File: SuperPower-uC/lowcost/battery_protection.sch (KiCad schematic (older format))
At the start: 7 parts, among them J1 Battery connector, J7 Battery connector, U1 FS312F-G, U2 FS8205A

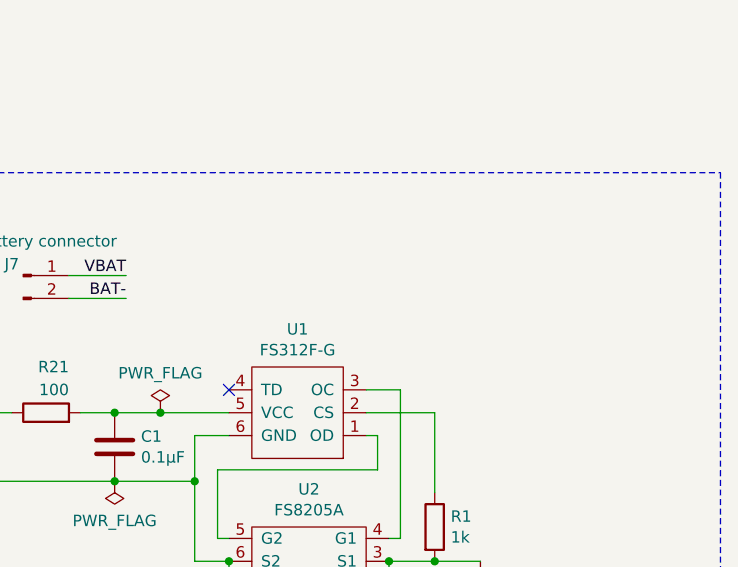
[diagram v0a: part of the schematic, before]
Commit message: added jumper to skip battery protection
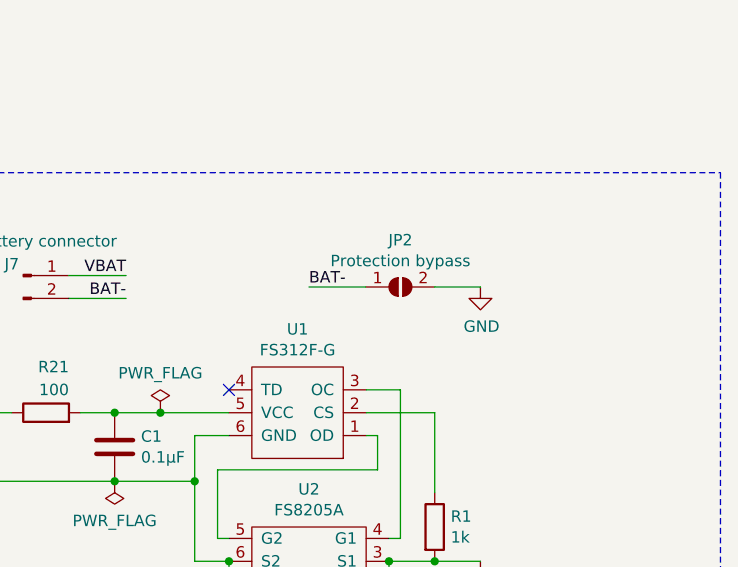
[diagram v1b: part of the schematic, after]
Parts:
- added JP2: Protection bypass, Jumper:SolderJumper-2_P1.3mm_Open_Pad1.0x1.5mm, symbol Jumper:SolderJumper_2_Open
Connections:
- net BAT-: now also JP2.1 (A)
- net GND: now also JP2.2 (B)
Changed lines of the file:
@@
 	5300 3550 5300 3900
-Wire Wire Line
-	6350 3900 6150 3900
 Wire Wire Line
 	6150 4000 6150 3900
@@
 Wire Wire Line
 	4050 3550 4950 3550
+$Comp
+L Jumper:SolderJumper_2_Open JP?
+U 1 1 5FFB2253
+P 6200 2700
+AR Path="/5F63A00B/5FFB2253" Ref="JP?"  Part="1"
+AR Path="/5F639CFE/5FFB2253" Ref="JP2"  Part="1"
+F 0 "JP2" H 6200 2905 50  0000 C CNN
+F 1 "Protection bypass" H 6200 2814 50  0000 C CNN
+F 2 "Jumper:SolderJumper-2_P1.3mm_Open_Pad1.0x1.5mm" H 6200 2700 50  0001 C CNN
+F 3 "~" H 6200 2700 50  0001 C CNN
+	1    6200 2700
+	1    0    0    -1
+$EndComp
+Wire Wire Line
+	6350 3900 6150 3900
+Text Label 5800 2700 0    50   ~ 0
+BAT-
+Wire Wire Line
+	5800 2700 6050 2700
+$Comp
+L power:GND #PWR?
+U 1 1 5FFB56AA
+P 6550 2700
+F 0 "#PWR?" H 6550 2450 50  0001 C CNN
+F 1 "GND" H 6555 2527 50  0000 C CNN
+F 2 "" H 6550 2700 50  0001 C CNN
+F 3 "" H 6550 2700 50  0001 C CNN
+	1    6550 2700
+	1    0    0    -1
+$EndComp
+Wire Wire Line
+	6550 2700 6350 2700
 $EndSCHEMATC

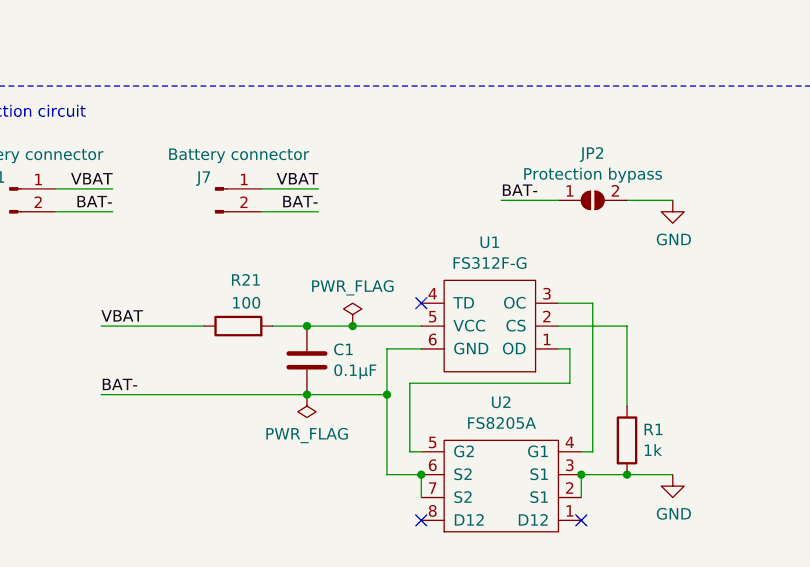
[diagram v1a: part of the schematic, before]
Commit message: swapped the proteciton ic for the AP9101CK6-ADTRG1
+ self recovery
+ reverse protection
- lower cutoff (due to availability by jlc)
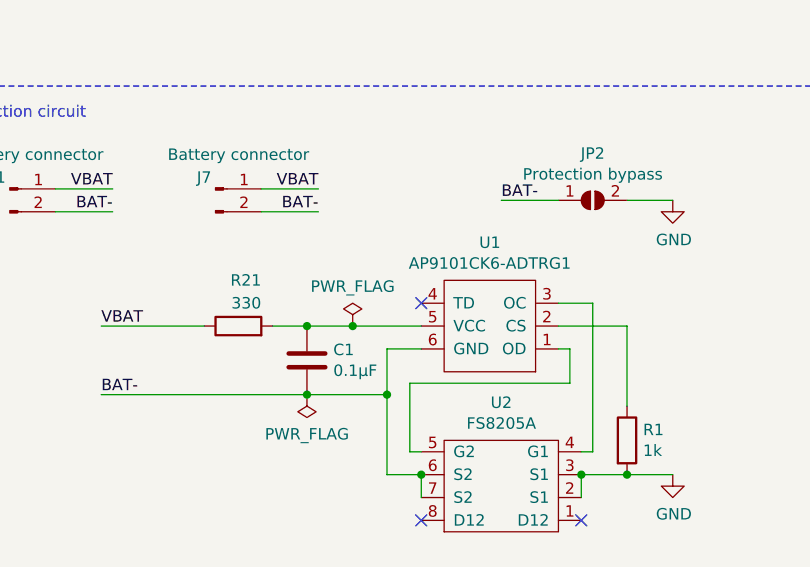
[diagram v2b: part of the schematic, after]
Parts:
- R21: value 100 -> 330; LCSC C22775 -> C23138
- U1: value FS312F-G -> AP9101CK6-ADTRG1; LCSC C82736 -> C151339
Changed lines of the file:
@@
 P 5750 3350
 F 0 "U1" H 5750 2885 50  0000 C CNN
-F 1 "FS312F-G" H 5750 2976 50  0000 C CNN
+F 1 "AP9101CK6-ADTRG1" H 5750 2976 50  0000 C CNN
 F 2 "Package_TO_SOT_SMD:SOT-23-6_Handsoldering" H 5850 3800 50  0001 C CNN
-F 3 "https://www.ic-fortune.com/upload/Download/FS312F-G-DS-12_EN.pdf" H 5750 3100 50  0001 C CNN
-F 4 "C82736" H 5750 3350 50  0001 C CNN "LCSC"
+F 3 "https://www.diodes.com/assets/Datasheets/AP9101C.pdf" H 5750 3100 50  0001 C CNN
+F 4 "C151339" H 5750 3350 50  0001 C CNN "LCSC"
 	1    5750 3350
 	-1   0    0    1
@@
 P 4650 3250
 F 0 "R21" V 4850 3150 50  0000 L CNN
-F 1 "100" V 4750 3150 50  0000 L CNN
+F 1 "330" V 4750 3150 50  0000 L CNN
 F 2 "Resistor_SMD:R_0603_1608Metric_Pad1.05x0.95mm_HandSolder" V 4580 3250 50  0001 C CNN
 F 3 "~" H 4650 3250 50  0001 C CNN
-F 4 "C22775" H 4650 3250 50  0001 C CNN "LCSC"
+F 4 "C23138" H 4650 3250 50  0001 C CNN "LCSC"
 	1    4650 3250
 	0    -1   -1   0

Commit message: added BOM
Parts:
- J7: LCSC C157931 -> (none)
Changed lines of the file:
@@
 F 2 "Connector_PinSocket_2.54mm:PinSocket_1x02_P2.54mm_Vertical" H 4550 2650 50  0001 C CNN
 F 3 "" H 4550 2650 50  0001 C CNN
-F 4 "C157931" H 4550 2650 50  0001 C CNN "LCSC"
+F 4 "" H 4550 2650 50  0001 C CNN "LCSC"
 	1    4550 2650
 	1    0    0    -1
@@
 	5800 2700 6050 2700
 $Comp
-L power:GND #PWR?
+L power:GND #PWR0129
 U 1 1 5FFB56AA
 P 6550 2700
-F 0 "#PWR?" H 6550 2450 50  0001 C CNN
+F 0 "#PWR0129" H 6550 2450 50  0001 C CNN
 F 1 "GND" H 6555 2527 50  0000 C CNN
 F 2 "" H 6550 2700 50  0001 C CNN

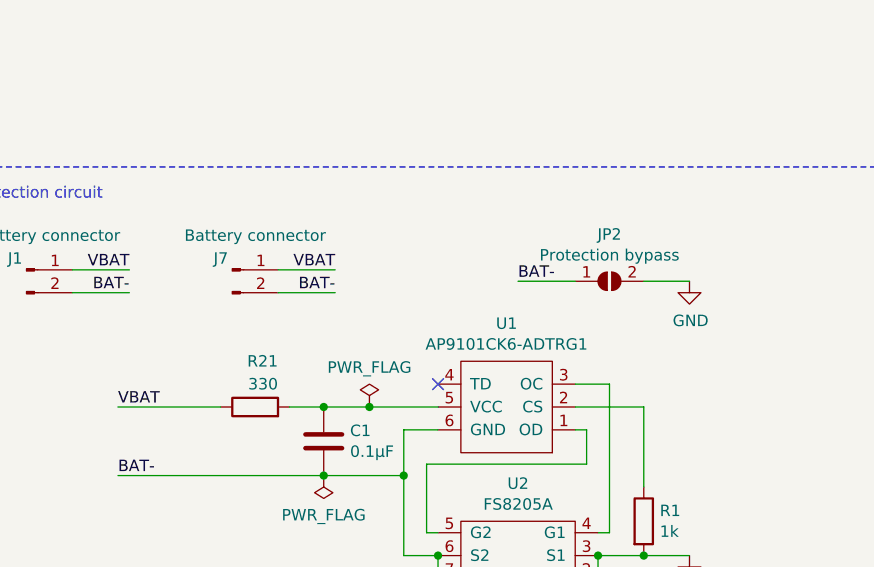
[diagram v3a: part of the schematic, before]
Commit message: swapped 2.54 with 2mm footprint and deleted jumper
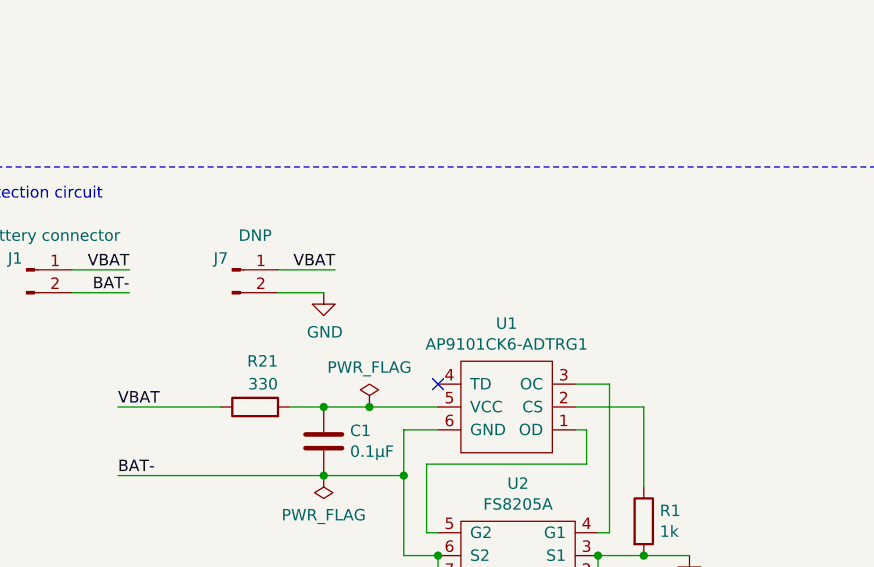
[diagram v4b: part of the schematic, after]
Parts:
- removed JP2: Protection bypass, Jumper:SolderJumper-2_P1.3mm_Open_Pad1.0x1.5mm, symbol Jumper:SolderJumper_2_Open
- J7: value Battery connector -> DNP; footprint Connector_PinSocket_2.54mm:PinSocket_1x02_P2.54mm_Vertical -> Connector_JST:JST_PH_S2B-PH-K_1x02_P2.00mm_Horizontal
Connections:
- net BAT-: no longer J7.2 (Pin_2)
- net GND: now also J7.2 (Pin_2)
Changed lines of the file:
@@
 Wire Wire Line
 	4050 3250 4500 3250
-$Comp
-L Connector:Conn_01x02_Male J7
-U 1 1 5FF3831A
-P 4550 2650
-F 0 "J7" H 4500 2700 50  0000 C CNN
-F 1 "Battery connector" H 4650 2800 50  0000 C CNN
-F 2 "Connector_PinSocket_2.54mm:PinSocket_1x02_P2.54mm_Vertical" H 4550 2650 50  0001 C CNN
-F 3 "" H 4550 2650 50  0001 C CNN
-F 4 "" H 4550 2650 50  0001 C CNN "LCSC"
-	1    4550 2650
-	1    0    0    -1
-$EndComp
 Text Label 5000 2650 2    50   ~ 0
 VBAT
@@
 Text Label 4100 2750 2    50   ~ 0
 BAT-
-Text Label 5000 2750 2    50   ~ 0
-BAT-
-Wire Wire Line
-	5000 2750 4750 2750
 Wire Wire Line
 	3850 2750 4100 2750
@@
 Wire Wire Line
 	4050 3550 4950 3550
+Wire Wire Line
+	6350 3900 6150 3900
 $Comp
-L Jumper:SolderJumper_2_Open JP?
-U 1 1 5FFB2253
-P 6200 2700
-AR Path="/5F63A00B/5FFB2253" Ref="JP?"  Part="1"
-AR Path="/5F639CFE/5FFB2253" Ref="JP2"  Part="1"
-F 0 "JP2" H 6200 2905 50  0000 C CNN
-F 1 "Protection bypass" H 6200 2814 50  0000 C CNN
-F 2 "Jumper:SolderJumper-2_P1.3mm_Open_Pad1.0x1.5mm" H 6200 2700 50  0001 C CNN
-F 3 "~" H 6200 2700 50  0001 C CNN
-	1    6200 2700
+L Connector:Conn_01x02_Male J7
+U 1 1 60035EFF
+P 4550 2650
+F 0 "J7" H 4500 2700 50  0000 C CNN
+F 1 "DNP" H 4650 2800 50  0000 C CNN
+F 2 "Connector_JST:JST_PH_S2B-PH-K_1x02_P2.00mm_Horizontal" H 4550 2650 50  0001 C CNN
+F 3 "" H 4550 2650 50  0001 C CNN
+F 4 "" H 4550 2650 50  0001 C CNN "LCSC"
+	1    4550 2650
+	1    0    0    -1
+$EndComp
+$Comp
+L power:GND #PWR0129
+U 1 1 60037B5A
+P 4950 2750
+F 0 "#PWR0129" H 4950 2500 50  0001 C CNN
+F 1 "GND" H 4955 2577 50  0000 C CNN
+F 2 "" H 4950 2750 50  0001 C CNN
+F 3 "" H 4950 2750 50  0001 C CNN
+	1    4950 2750
 	1    0    0    -1
 $EndComp
 Wire Wire Line
-	6350 3900 6150 3900
-Text Label 5800 2700 0    50   ~ 0
-BAT-
-Wire Wire Line
-	5800 2700 6050 2700
-$Comp
-L power:GND #PWR0129
-U 1 1 5FFB56AA
-P 6550 2700
-F 0 "#PWR0129" H 6550 2450 50  0001 C CNN
-F 1 "GND" H 6555 2527 50  0000 C CNN
-F 2 "" H 6550 2700 50  0001 C CNN
-F 3 "" H 6550 2700 50  0001 C CNN
-	1    6550 2700
-	1    0    0    -1
-$EndComp
-Wire Wire Line
-	6550 2700 6350 2700
+	4950 2750 4750 2750
 $EndSCHEMATC
